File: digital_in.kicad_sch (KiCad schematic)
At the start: 18 parts, among them U1 AM26LV32xD

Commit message: Routed analog input and generator, added ethernet
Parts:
- D1, D2, D3, D4: value SM712_SOT23 -> TVS
- U1: value AM26LV32xD -> AM26LV32
- renumbered R6 to R1, R12 to R10, R4 to R11, R13 to R12, R1 to R2, R7 to R3, R8 to R4, R2 to R5, R9 to R6, R10 to R7, R3 to R8, R11 to R9

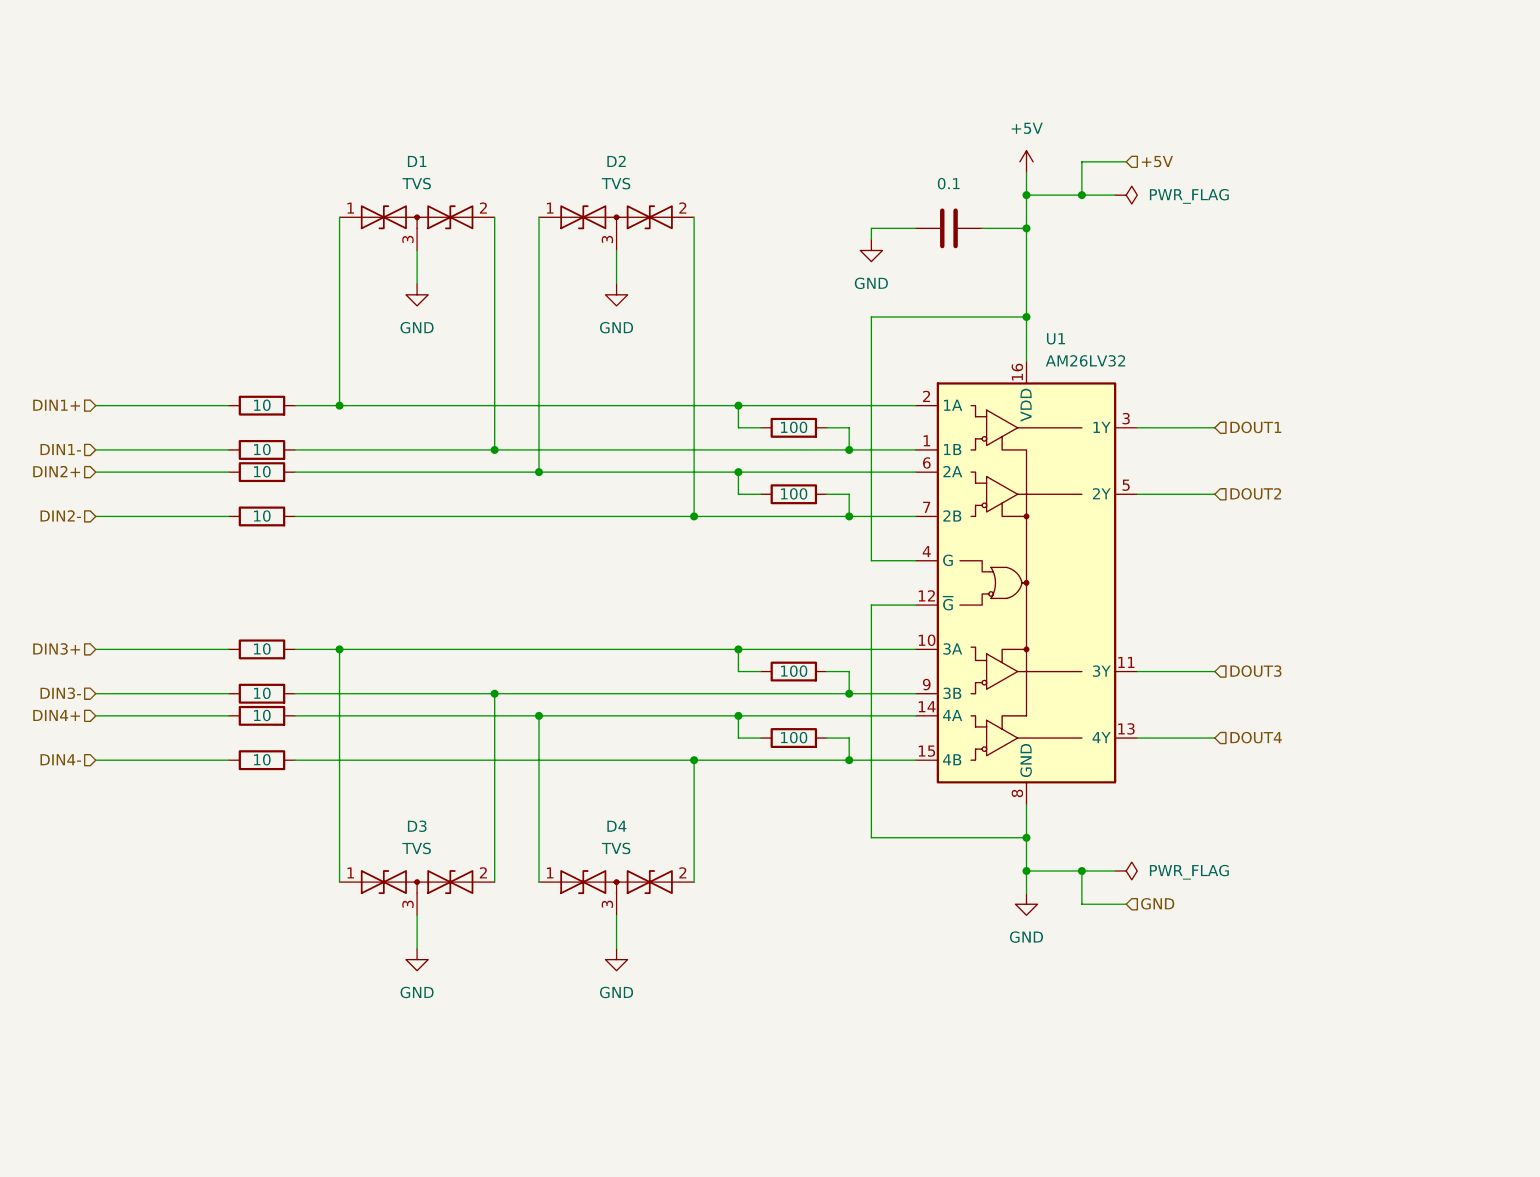
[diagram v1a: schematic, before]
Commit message: Rearranged sheets and corrected some namings
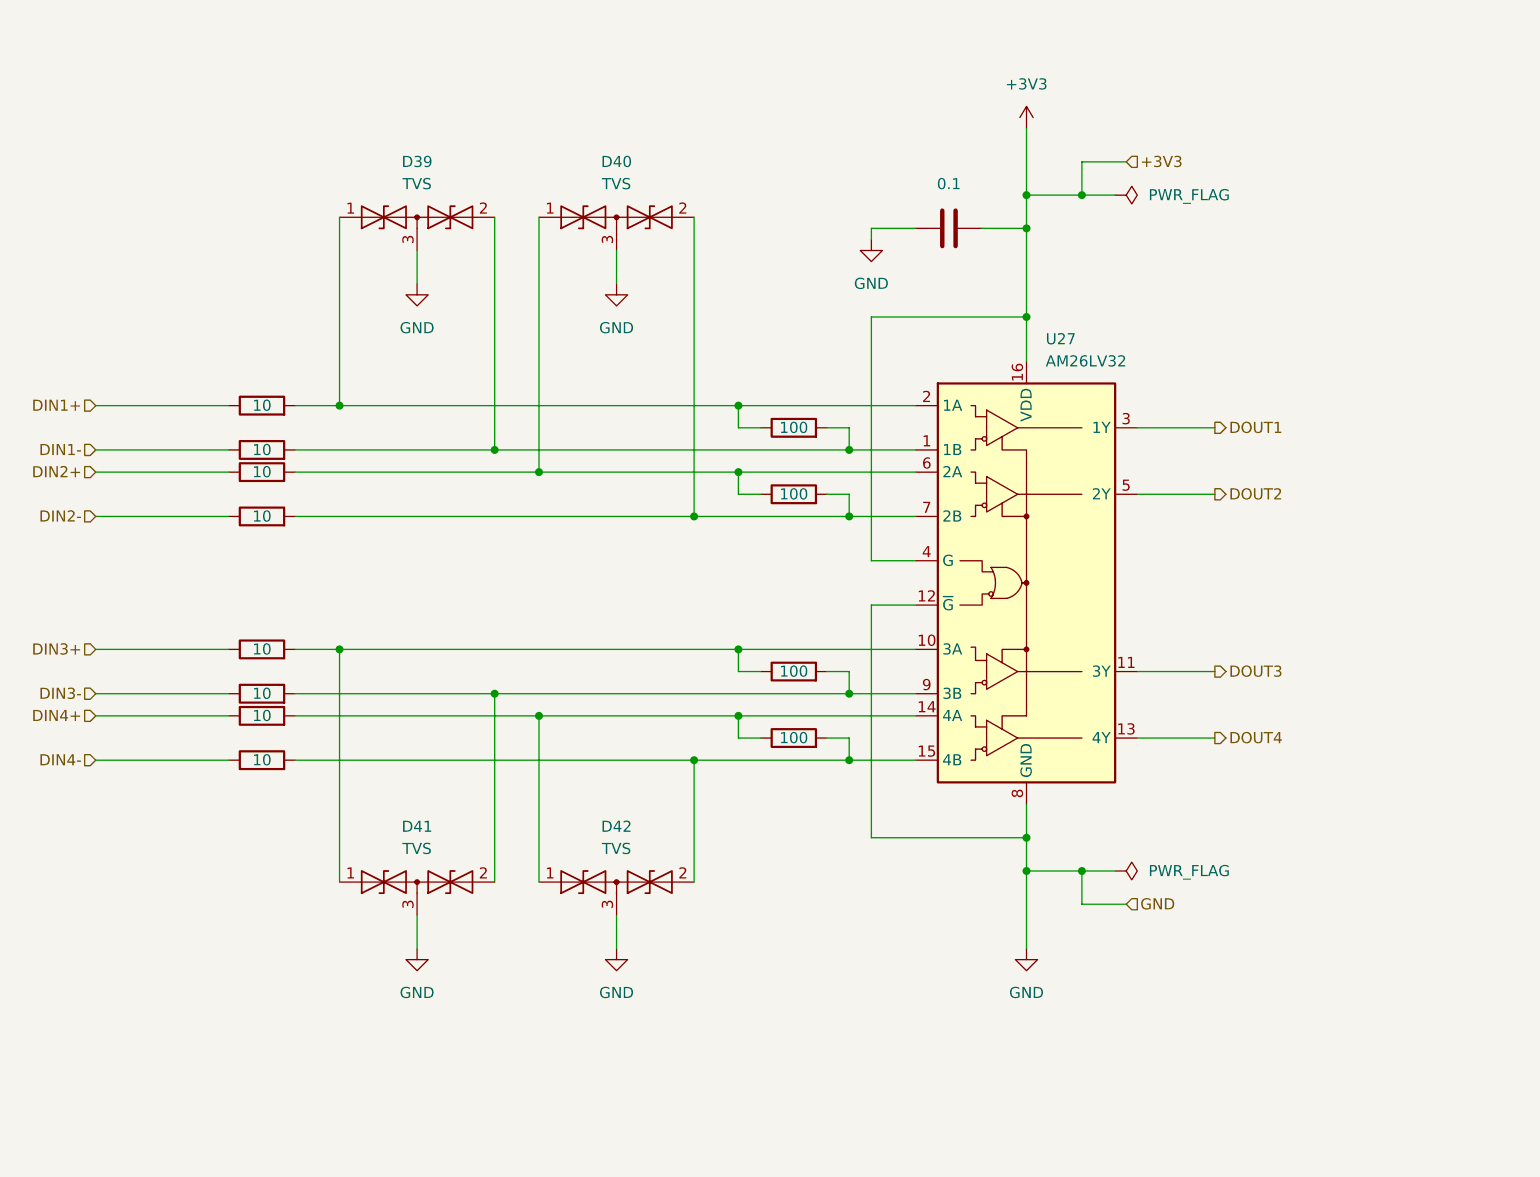
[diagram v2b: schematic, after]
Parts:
- renumbered C1 to C49, D1 to D39, D2 to D40, D3 to D41, D4 to D42, R1 to R143, R2 to R144, R3 to R145, R4 to R146, R5 to R147, R6 to R148, R7 to R149, R8 to R150, R9 to R151, R10 to R152, R11 to R153, R12 to R154, U1 to U27
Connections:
- net +5V renamed +3V3

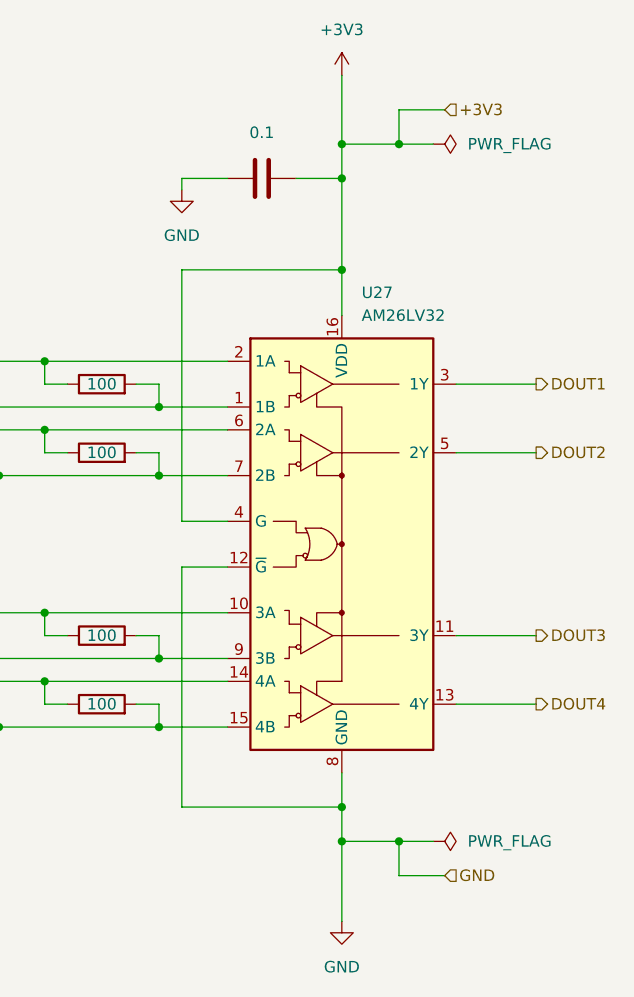
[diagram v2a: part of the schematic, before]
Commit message: Finished power setup and cleared some mistakes
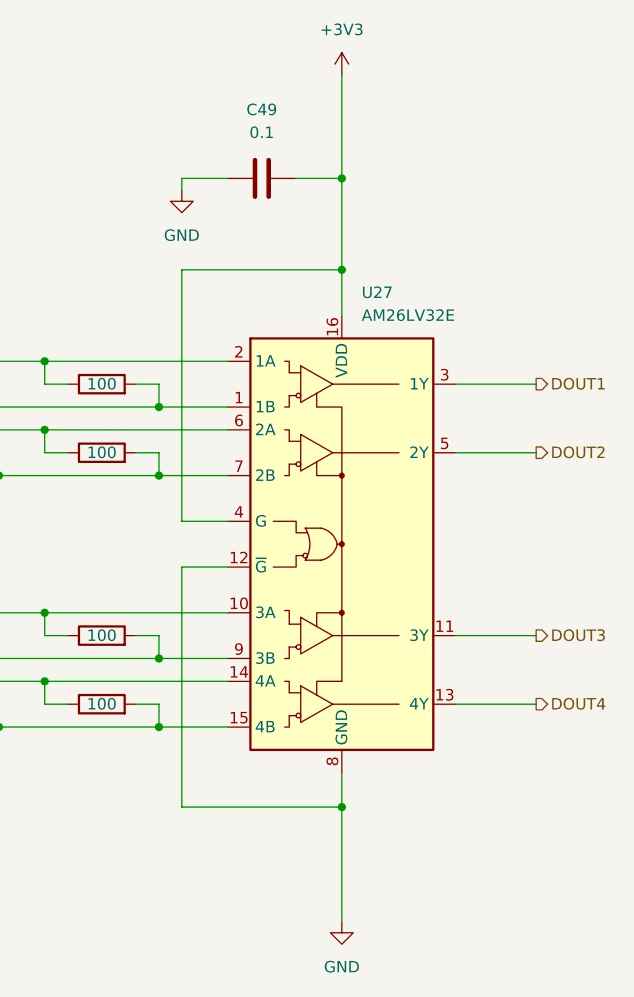
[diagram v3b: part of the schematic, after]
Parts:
- U27: value AM26LV32 -> AM26LV32E
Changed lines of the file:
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@@
 (kicad_sch (version 20230121) (generator eeschema)
   (paper "A4")
-  (junction (at 193.04 130.81) (diameter 0) (color 0 0 0 0)
-  )
   (junction (at 160.02 85.09) (diameter 0) (color 0 0 0 0)
   )
@@
   (junction (at 160.02 77.47) (diameter 0) (color 0 0 0 0)
   )
-  (junction (at 199.39 53.34) (diameter 0) (color 0 0 0 0)
-  )
   (junction (at 132.08 110.49) (diameter 0) (color 0 0 0 0)
   )
@@
   (junction (at 154.94 90.17) (diameter 0) (color 0 0 0 0)
   )
-  (junction (at 199.39 130.81) (diameter 0) (color 0 0 0 0)
-  )
   (junction (at 114.3 77.47) (diameter 0) (color 0 0 0 0)
   )
@@
   (junction (at 137.16 85.09) (diameter 0) (color 0 0 0 0)
   )
-  (junction (at 193.04 53.34) (diameter 0) (color 0 0 0 0)
-  )
   (junction (at 160.02 105.41) (diameter 0) (color 0 0 0 0)
   )
@@
     (stroke (width 0) (type default))
   )
-  (wire (pts (xy 193.04 53.34) (xy 193.04 57.15))
+  (wire (pts (xy 193.04 45.72) (xy 193.04 57.15))
     (stroke (width 0) (type default))
   )
@@
     (stroke (width 0) (type default))
   )
-  (wire (pts (xy 193.04 130.81) (xy 193.04 139.7))
-    (stroke (width 0) (type default))
-  )
   (wire (pts (xy 109.22 113.03) (xy 137.16 113.03))
     (stroke (width 0) (type default))
@@
     (stroke (width 0) (type default))
   )
-  (wire (pts (xy 199.39 53.34) (xy 193.04 53.34))
-    (stroke (width 0) (type default))
-  )
-  (wire (pts (xy 204.47 134.62) (xy 199.39 134.62))
-    (stroke (width 0) (type default))
-  )
   (wire (pts (xy 86.36 113.03) (xy 101.6 113.03))
     (stroke (width 0) (type default))
@@
     (stroke (width 0) (type default))
   )
-  (wire (pts (xy 193.04 45.72) (xy 193.04 53.34))
-    (stroke (width 0) (type default))
-  )
   (wire (pts (xy 193.04 123.19) (xy 193.04 127))
     (stroke (width 0) (type default))
@@
     (stroke (width 0) (type default))
   )
-  (wire (pts (xy 199.39 134.62) (xy 199.39 130.81))
-    (stroke (width 0) (type default))
-  )
   (wire (pts (xy 114.3 105.41) (xy 114.3 132.08))
     (stroke (width 0) (type default))
@@
     (stroke (width 0) (type default))
   )
-  (wire (pts (xy 193.04 127) (xy 193.04 130.81))
+  (wire (pts (xy 193.04 127) (xy 193.04 139.7))
     (stroke (width 0) (type default))
   )
@@
     (stroke (width 0) (type default))
   )
-  (wire (pts (xy 203.2 53.34) (xy 199.39 53.34))
-    (stroke (width 0) (type default))
-  )
   (wire (pts (xy 205.74 87.63) (xy 214.63 87.63))
     (stroke (width 0) (type default))
@@
     (stroke (width 0) (type default))
   )
-  (wire (pts (xy 204.47 49.53) (xy 199.39 49.53))
-    (stroke (width 0) (type default))
-  )
   (wire (pts (xy 205.74 107.95) (xy 214.63 107.95))
     (stroke (width 0) (type default))
@@
     (stroke (width 0) (type default))
   )
-  (wire (pts (xy 199.39 130.81) (xy 193.04 130.81))
-    (stroke (width 0) (type default))
-  )
   (wire (pts (xy 132.08 110.49) (xy 132.08 132.08))
     (stroke (width 0) (type default))
@@
     (stroke (width 0) (type default))
   )
-  (wire (pts (xy 203.2 130.81) (xy 199.39 130.81))
-    (stroke (width 0) (type default))
-  )
   (wire (pts (xy 205.74 115.57) (xy 214.63 115.57))
     (stroke (width 0) (type default))
@@
   )
   (wire (pts (xy 132.08 55.88) (xy 132.08 82.55))
-    (stroke (width 0) (type default))
-  )
-  (wire (pts (xy 199.39 49.53) (xy 199.39 53.34))
     (stroke (width 0) (type default))
   )
@@
     (effects (font (size 1.27 1.27)) (justify right))
   )
-  (hierarchical_label "GND" (shape input) (at 204.47 134.62 0) (fields_autoplaced)
-    (effects (font (size 1.27 1.27)) (justify left))
-  )
   (hierarchical_label "DIN2-" (shape input) (at 86.36 90.17 180) (fields_autoplaced)
     (effects (font (size 1.27 1.27)) (justify right))
@@
   )
   (hierarchical_label "DOUT3" (shape output) (at 214.63 107.95 0) (fields_autoplaced)
-    (effects (font (size 1.27 1.27)) (justify left))
-  )
-  (hierarchical_label "+3V3" (shape input) (at 204.47 49.53 0) (fields_autoplaced)
     (effects (font (size 1.27 1.27)) (justify left))
   )
@@
     (in_bom yes) (on_board yes) (dnp no) (fields_autoplaced)
     (property "Reference" "C49" (at 184.15 49.53 90)
-      (effects (font (size 1.27 1.27)) hide)
+      (effects (font (size 1.27 1.27)))
     )
     (property "Value" "0.1" (at 184.15 52.07 90)
@@
         (path "/894df1c3-1a5d-48b0-9966-84d5c2c2c705/73a9a112-2b13-45e0-9846-6d7d5c23fe7b"
           (reference "R140") (unit 1)
-        )
-      )
-    )
-  )
-  (symbol (lib_id "power:PWR_FLAG") (at 203.2 53.34 270) (unit 1)
-    (in_bom yes) (on_board yes) (dnp no) (fields_autoplaced)
-    (property "Reference" "#FLG059" (at 205.105 53.34 0)
-      (effects (font (size 1.27 1.27)) hide)
-    )
-    (property "Value" "PWR_FLAG" (at 207.01 53.34 90)
-      (effects (font (size 1.27 1.27)) (justify left))
-    )
-    (property "Footprint" "" (at 203.2 53.34 0)
-      (effects (font (size 1.27 1.27)) hide)
-    )
-    (property "Datasheet" "~" (at 203.2 53.34 0)
-      (effects (font (size 1.27 1.27)) hide)
-    )
-    (pin "1")
-    (instances
-      (project "cad-enc-dec"
-        (path "/894df1c3-1a5d-48b0-9966-84d5c2c2c705/d5ddf39e-f446-4bb3-803c-3c40992ae5b8"
-          (reference "#FLG059") (unit 1)
-        )
-        (path "/894df1c3-1a5d-48b0-9966-84d5c2c2c705/51663df1-c19b-4b22-937a-7e356ec35286"
-          (reference "#FLG045") (unit 1)
-        )
-        (path "/894df1c3-1a5d-48b0-9966-84d5c2c2c705/65dbfbbd-5781-4a33-9d09-f40cb40152c2"
-          (reference "#FLG051") (unit 1)
-        )
-        (path "/894df1c3-1a5d-48b0-9966-84d5c2c2c705/89c877e3-9585-4510-b310-dcd1e60248c3"
-          (reference "#FLG01") (unit 1)
-        )
-        (path "/894df1c3-1a5d-48b0-9966-84d5c2c2c705/0403abf9-0495-408c-afe9-82193f47d579"
-          (reference "#FLG047") (unit 1)
-        )
-        (path "/894df1c3-1a5d-48b0-9966-84d5c2c2c705/0af0c5a3-3a5c-4c44-8d89-26655ad3bf82"
-          (reference "#FLG049") (unit 1)
-        )
-        (path "/894df1c3-1a5d-48b0-9966-84d5c2c2c705/1be909cf-e514-4127-9457-3b38ed6871c4"
-          (reference "#FLG053") (unit 1)
-        )
-        (path "/894df1c3-1a5d-48b0-9966-84d5c2c2c705/4af69132-85f4-4331-8f4a-e2734fd52655"
-          (reference "#FLG055") (unit 1)
-        )
-        (path "/894df1c3-1a5d-48b0-9966-84d5c2c2c705/73a9a112-2b13-45e0-9846-6d7d5c23fe7b"
-          (reference "#FLG057") (unit 1)
         )
       )
@@
       (effects (font (size 1.27 1.27)) (justify left))
     )
-    (property "Value" "AM26LV32" (at 195.2341 72.39 0)
+    (property "Value" "AM26LV32E" (at 195.2341 72.39 0)
       (effects (font (size 1.27 1.27)) (justify left))
     )
@@
         )
       )
-    )
-  )
-  (symbol (lib_id "power:PWR_FLAG") (at 203.2 130.81 270) (unit 1)
-    (in_bom yes) (on_board yes) (dnp no) (fields_autoplaced)
-    (property "Reference" "#FLG060" (at 205.105 130.81 0)
-      (effects (font (size 1.27 1.27)) hide)
-    )
-    (property "Value" "PWR_FLAG" (at 207.01 130.81 90)
-      (effects (font (size 1.27 1.27)) (justify left))
-    )
-    (property "Footprint" "" (at 203.2 130.81 0)
-      (effects (font (size 1.27 1.27)) hide)
-    )
-    (property "Datasheet" "~" (at 203.2 130.81 0)
-      (effects (font (size 1.27 1.27)) hide)
-    )
-    (pin "1")
-    (instances
-      (project "cad-enc-dec"
-        (path "/894df1c3-1a5d-48b0-9966-84d5c2c2c705/d5ddf39e-f446-4bb3-803c-3c40992ae5b8"
-          (reference "#FLG060") (unit 1)
-        )
-        (path "/894df1c3-1a5d-48b0-9966-84d5c2c2c705/51663df1-c19b-4b22-937a-7e356ec35286"
-          (reference "#FLG046") (unit 1)
-        )
-        (path "/894df1c3-1a5d-48b0-9966-84d5c2c2c705/65dbfbbd-5781-4a33-9d09-f40cb40152c2"
-          (reference "#FLG052") (unit 1)
-        )
-        (path "/894df1c3-1a5d-48b0-9966-84d5c2c2c705/89c877e3-9585-4510-b310-dcd1e60248c3"
-          (reference "#FLG02") (unit 1)
-        )
-        (path "/894df1c3-1a5d-48b0-9966-84d5c2c2c705/0403abf9-0495-408c-afe9-82193f47d579"
-          (reference "#FLG048") (unit 1)
-        )
-        (path "/894df1c3-1a5d-48b0-9966-84d5c2c2c705/0af0c5a3-3a5c-4c44-8d89-26655ad3bf82"
-          (reference "#FLG050") (unit 1)
-        )
-        (path "/894df1c3-1a5d-48b0-9966-84d5c2c2c705/1be909cf-e514-4127-9457-3b38ed6871c4"
-          (reference "#FLG054") (unit 1)
-        )
-        (path "/894df1c3-1a5d-48b0-9966-84d5c2c2c705/4af69132-85f4-4331-8f4a-e2734fd52655"
-          (reference "#FLG056") (unit 1)
-        )
-        (path "/894df1c3-1a5d-48b0-9966-84d5c2c2c705/73a9a112-2b13-45e0-9846-6d7d5c23fe7b"
-          (reference "#FLG058") (unit 1)
-        )
-      )
